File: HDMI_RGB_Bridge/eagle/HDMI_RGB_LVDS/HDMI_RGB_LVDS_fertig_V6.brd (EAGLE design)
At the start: 70 x 60 mm, 91 parts, among them CON1 KLDX-0202-A-LT, CON2 FCI-10029449-111RLF, CON3 XF2M-4015-1A, CON4 FCI-10033526-N3212LF, CON5 MOLEX-53261-0671, CON6 FI-X30SSLA-HF, IC2 WPMDL1300331BD, IC4 AT24C01C-SSHM-B, IC5 TFP401APZP, IC6 ATMEGA48A-AU, IC7 FT232RL, IC8 SN75LVDS83BDGGR, Q1 ATS073ASM-1, T1 IRLML5203TRPBF, T2 IRLML2502TRPBF

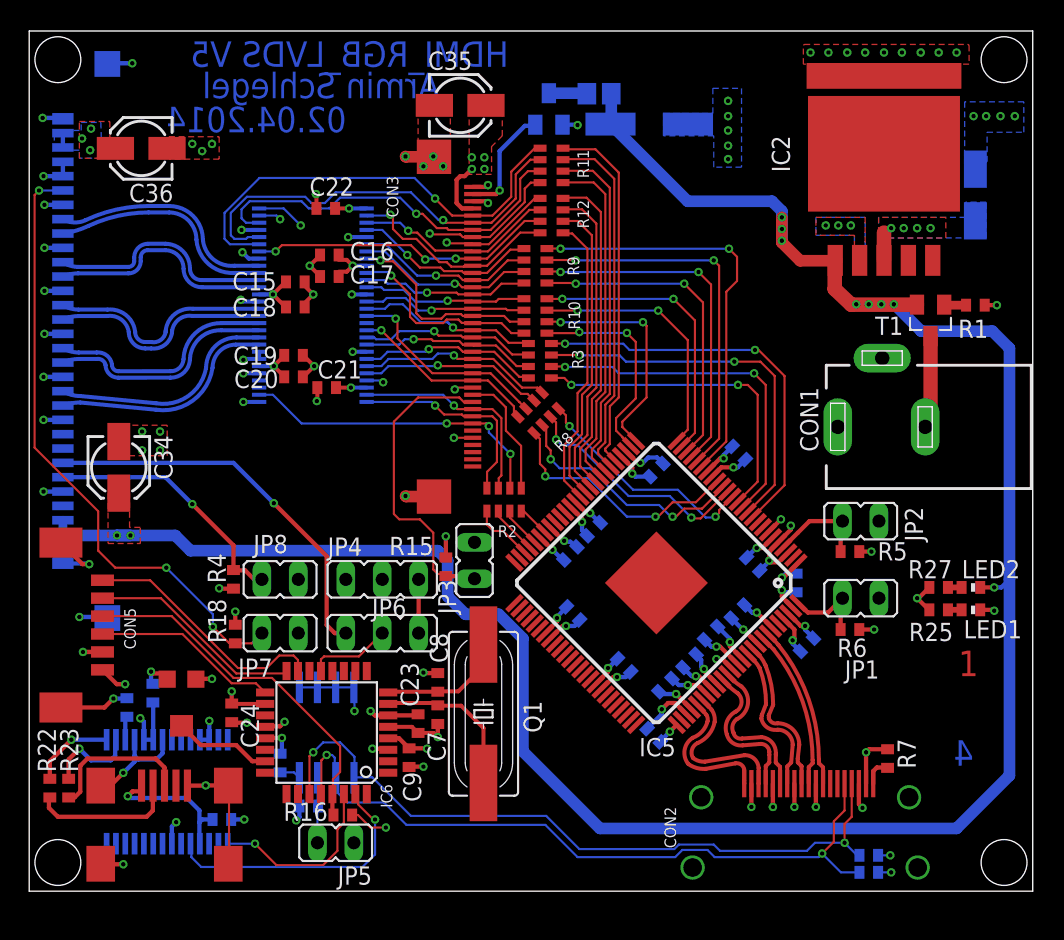
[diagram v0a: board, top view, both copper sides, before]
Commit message: writing and reading to eeprom works - checksum needs to be fixed
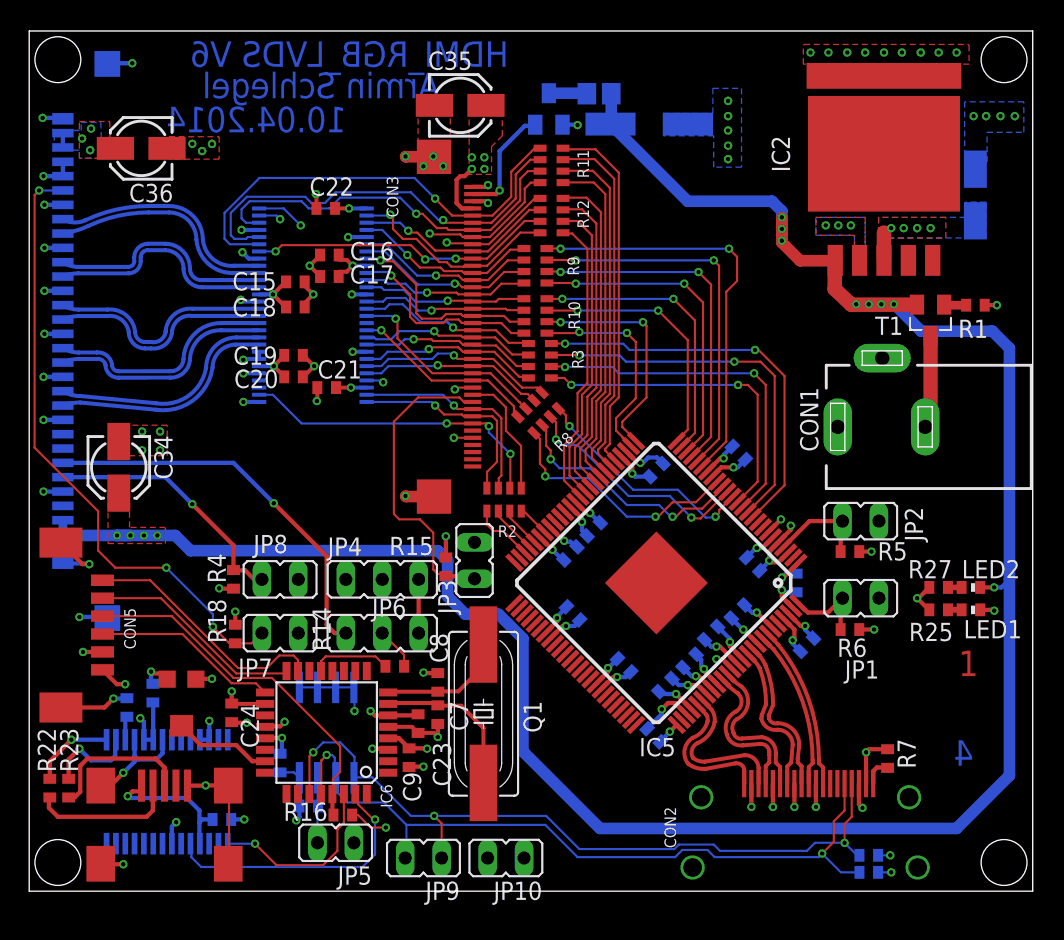
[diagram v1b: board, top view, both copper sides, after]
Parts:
- added JP10, JP9: JUMPER2, SchlegelAr_Master:JUMPER2_THROUGHHOLE
- added R14: 22R, SchlegelAr_Master:R0402
- C16, C18, C20: value 0.1u -> 100n
- IC6: value ATMEGA48A-AU -> ATMEGA88PA
- R19: value 10k -> 5k
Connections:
- new net N$1: IC6.13, R14.1
- net +5V: now also JP10.2
- net AVR_PWM: now also R14.2; no longer IC6.13
- net EDID_SCL: now also JP9.2
- net EDID_SDA: now also JP9.1
- net GND: now also JP10.1
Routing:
- net N$1: track 0.00 -> 5.61 mm
- net EDID_SDA: track 50.6 -> 53.8 mm, vias 2 -> 3
- net AVR_PWM: track 5.84 -> 2.94 mm
- net EDID_SCL: track 50.9 -> 53.3 mm
- net +12V: vias 10 -> 12
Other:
- board text added: "10.04.2014"
- board text added: "HDMI_RGB_LVDS V6"
- board text removed: "02.04.2014"
- board text removed: "HDMI_RGB_LVDS V5"
